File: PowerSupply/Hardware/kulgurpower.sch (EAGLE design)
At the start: 138 parts, among them M1 MST2V, M2 MST2V, M3 MST2V, M4 MST2V, X1 1727036, X2 2534-, X3 22-23-2031, X4 22-23-2031, X5 22-23-2021

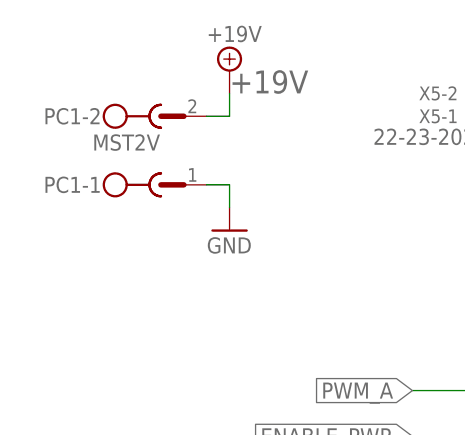
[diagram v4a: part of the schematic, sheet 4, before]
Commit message: Silkscreen fixes
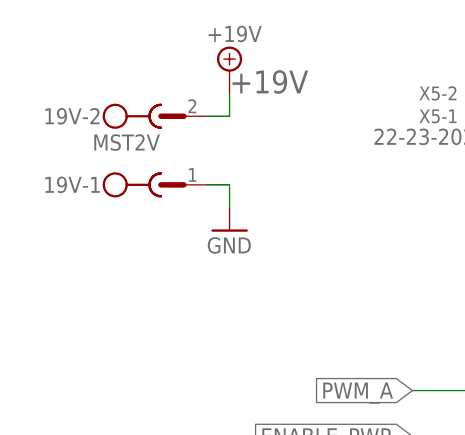
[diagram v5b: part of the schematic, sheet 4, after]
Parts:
- renumbered PC1 to 19V
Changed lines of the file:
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@@
 <part name="C15" library="rcl" deviceset="CPOL-EU" device="C/6032-28R"/>
 <part name="C30" library="rcl" deviceset="CPOL-EU" device="C/6032-28R"/>
-<part name="PC1" library="con-phoenix-508" deviceset="MST2V" device=""/>
+<part name="19V" library="con-phoenix-508" deviceset="MST2V" device=""/>
 <part name="SUPPLY6" library="supply2" deviceset="+18V" device="" value="+19V"/>
 <part name="GND52" library="supply1" deviceset="GND" device=""/>
@@
 <instance part="X5" gate="-2" x="101.6" y="157.48" rot="R180"/>
 <instance part="GND29" gate="1" x="106.68" y="149.86"/>
-<instance part="PC1" gate="-1" x="66.04" y="147.32"/>
-<instance part="PC1" gate="-2" x="66.04" y="154.94"/>
+<instance part="19V" gate="-1" x="66.04" y="147.32"/>
+<instance part="19V" gate="-2" x="66.04" y="154.94"/>
 <instance part="SUPPLY6" gate="+18V" x="73.66" y="160.02"/>
 <instance part="GND52" gate="1" x="73.66" y="142.24"/>
@@
 <pinref part="SUPPLY6" gate="+18V" pin="+18V"/>
 <label x="73.66" y="157.48" size="2.54" layer="95"/>
-<pinref part="PC1" gate="-2" pin="1"/>
+<pinref part="19V" gate="-2" pin="1"/>
 <wire x1="73.66" y1="154.94" x2="71.12" y2="154.94" width="0.4064" layer="91"/>
 </segment>
@@
 </segment>
 <segment>
-<pinref part="PC1" gate="-1" pin="1"/>
+<pinref part="19V" gate="-1" pin="1"/>
 <pinref part="GND52" gate="1" pin="GND"/>
 <wire x1="71.12" y1="147.32" x2="73.66" y2="147.32" width="0.1524" layer="91"/>

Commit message: Minor fixes to PCB
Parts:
- removed C13, C14: (no value), rcl:CPOL-EUC/6032-28R
- added C31, C35: (no value), rcl:CPOL-EUC/6032-28R
- added C36, C37: 15V, rcl:CPOL-EUC/6032-28R
- added C38: 15V, rcl:CPOL-EU175TMP-0810
- added C39: 15v, rcl:CPOL-EU175TMP-0810
- added D4: MBRS330T3, diode:MBRS330T3
- added PAD1, PAD2, PAD3, PAD4, PAD5, PAD6, PAD7, PAD8: (no value), wirepad:1,6/0,9
- C104, C113, C32: value 220n -> 0.1
- C3: value (none) -> 15V
- L1, L2: device inductors:DR73 -> inductors:DR125
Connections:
- net 5V renamed 5V_LDO
- new net +19V_CHG: D4.C, X2-14.KL, X2-16.KL
- new net N$2: D4.A
- net +19V: no longer X2-14.KL, X2-16.KL
- net +5V: now also C31.+, C35.+; no longer C13.+
- net GND: now also C31.-, C35.-, C36.-, C37.-, C38.-, C39.-; no longer C13.-, C14.-
- net SERVO: no longer C14.+
- net V+: now also C36.+, C37.+, C38.+, C39.+
- net VBAT0: no longer X2-1.KL, X2-2.KL
- net VBAT0_X: now also PAD1.P, PAD8.P, X2-1.KL, X2-2.KL
- net VBAT1: no longer X2-3.KL, X2-4.KL
- net VBAT1_X: now also PAD2.P, PAD7.P, X2-3.KL, X2-4.KL
- net VBAT2: no longer X2-5.KL, X2-6.KL
- net VBAT2_X: now also PAD3.P, PAD6.P, X2-5.KL, X2-6.KL
- net VBAT3: no longer X2-7.KL, X2-8.KL
- net VBAT3_X: now also PAD4.P, PAD5.P, X2-7.KL, X2-8.KL
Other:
- note added: "Hack! !ON! pin of MAX1614 is pulled up by default. Pulling it down enables power. This is achieved using shorting power socket with special tool. Diodes D1, D3 avoid 19V from adapter to flow into !ON! pin which is droven by MCU. D4 avoids flowing LiPo voltage to 19V socket."
- note removed: "Hack! !ON! pin of MAX1614 is pulled up by default. Pulling it down enables power. This is achieved using shorting power socket with special tool. Diodes avoid 19V from adapter to flow into !ON! pin which is droven by MCU."
- moved on the sheet: 19V-1, 19V-2, C1, C10, C113, C15, C16, C17, C2, C20, C21, C25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

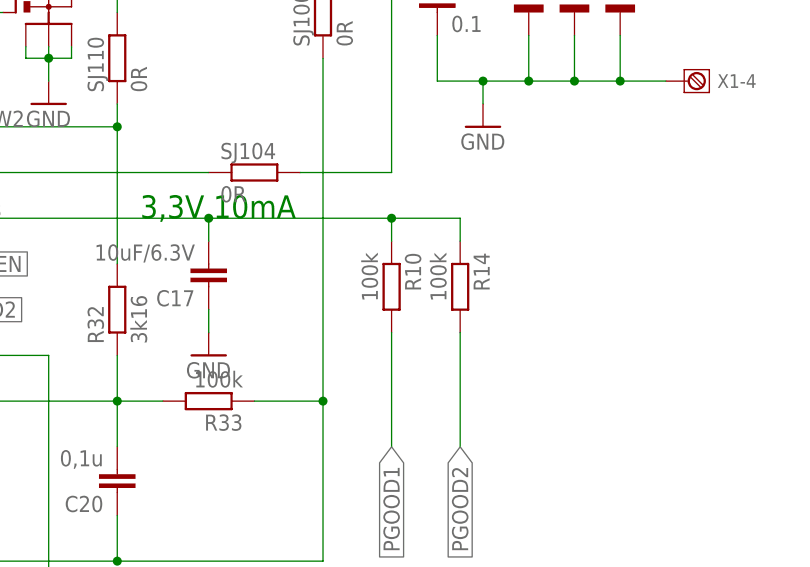
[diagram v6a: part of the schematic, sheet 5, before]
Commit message: Two resistors in ladder were swapped Nominals rised for pullup. Next power bill will be smaller!
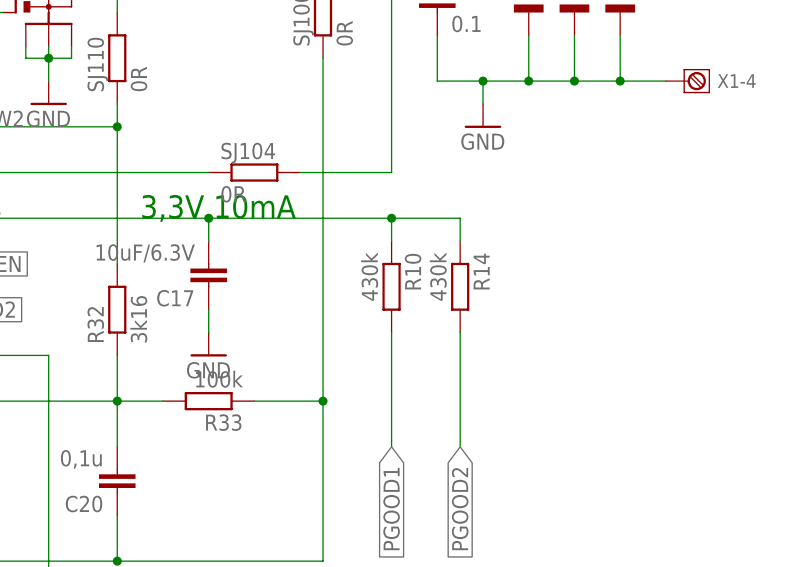
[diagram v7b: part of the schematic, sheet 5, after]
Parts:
- R10, R14: value 100k -> 430k
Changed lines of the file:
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@@
 <part name="X5" library="con-molex" deviceset="22-23-2021" device=""/>
 <part name="GND29" library="supply1" deviceset="GND" device=""/>
-<part name="R10" library="rcl" deviceset="R-EU_" device="R0603" value="100k"/>
-<part name="R14" library="rcl" deviceset="R-EU_" device="R0603" value="100k"/>
+<part name="R10" library="rcl" deviceset="R-EU_" device="R0603" value="430k"/>
+<part name="R14" library="rcl" deviceset="R-EU_" device="R0603" value="430k"/>
 <part name="C15" library="rcl" deviceset="CPOL-EU" device="C/6032-28R"/>
 <part name="C30" library="rcl" deviceset="CPOL-EU" device="C/6032-28R"/>

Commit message: PCB updates
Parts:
- C11, C18, C4, C7: value 0.1 -> 1n
- R25, R33: value 100k -> 3k9
- R31, R32: value 3k16 -> 10k
- R39: value 30k -> 24k
- R40: value 270k -> 143k
- R5: value 30k -> 24.3
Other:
- note added: "R1 = (VOUT -1.0) * R2 143 = 5.9 * 24.3"
- note removed: "R1 = (VOUT -1.0) * R2 270 = 9 * 30"
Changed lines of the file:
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@@
 <part name="U$4" library="SparkFun-AnalogIC" deviceset="ACS712" device=""/>
 <part name="GND5" library="supply1" deviceset="GND" device=""/>
-<part name="C7" library="rcl" deviceset="C-EU" device="C0603" value="0.1"/>
+<part name="C7" library="rcl" deviceset="C-EU" device="C0603" value="1n"/>
 <part name="GND15" library="supply1" deviceset="GND" device=""/>
 <part name="U$6" library="FDMS8558S" deviceset="FDMS8558S" device="" value="AON6500"/>
@@
 <part name="U$8" library="SparkFun-AnalogIC" deviceset="ACS712" device=""/>
 <part name="GND2" library="supply1" deviceset="GND" device=""/>
-<part name="C4" library="rcl" deviceset="C-EU" device="C0603" value="0.1"/>
+<part name="C4" library="rcl" deviceset="C-EU" device="C0603" value="1n"/>
 <part name="GND10" library="supply1" deviceset="GND" device=""/>
 <part name="U$9" library="FDMS8558S" deviceset="FDMS8558S" device="" value="AON6500"/>
@@
 <part name="U$11" library="SparkFun-AnalogIC" deviceset="ACS712" device=""/>
 <part name="GND12" library="supply1" deviceset="GND" device=""/>
-<part name="C11" library="rcl" deviceset="C-EU" device="C0603" value="0.1"/>
+<part name="C11" library="rcl" deviceset="C-EU" device="C0603" value="1n"/>
 <part name="GND18" library="supply1" deviceset="GND" device=""/>
 <part name="U$5" library="FDMS8558S" deviceset="FDMS8558S" device="" value="AON6500"/>
@@
 <part name="U$13" library="SparkFun-AnalogIC" deviceset="ACS712" device=""/>
 <part name="GND23" library="supply1" deviceset="GND" device=""/>
-<part name="C18" library="rcl" deviceset="C-EU" device="C0603" value="0.1"/>
+<part name="C18" library="rcl" deviceset="C-EU" device="C0603" value="1n"/>
 <part name="GND34" library="supply1" deviceset="GND" device=""/>
 <part name="PC" library="con-phoenix-508" deviceset="MST2V" device=""/>
@@
 <part name="GND22" library="SparkFun" deviceset="GND" device="" value="GND"/>
 <part name="R3" library="rcl" deviceset="R-EU_" device="R0603" value="300k"/>
-<part name="R39" library="rcl" deviceset="R-EU_" device="R0603" value="30k"/>
+<part name="R39" library="rcl" deviceset="R-EU_" device="R0603" value="24k"/>
 <part name="R23" library="rcl" deviceset="R-EU_" device="R0603" value="18k"/>
 <part name="R4" library="rcl" deviceset="R-EU_" device="R0603" value="30k"/>
-<part name="R5" library="rcl" deviceset="R-EU_" device="R0603" value="30k"/>
+<part name="R5" library="rcl" deviceset="R-EU_" device="R0603" value="24.3"/>
 <part name="R21" library="rcl" deviceset="R-EU_" device="R0603" value="120k"/>
-<part name="R40" library="rcl" deviceset="R-EU_" device="R0603" value="270k"/>
+<part name="R40" library="rcl" deviceset="R-EU_" device="R0603" value="143k"/>
 <part name="C5" library="rcl" deviceset="C-EU" device="C1210" value="10u"/>
 <part name="GND25" library="SparkFun" deviceset="GND" device=""/>
@@
 <part name="GND50" library="SparkFun" deviceset="GND" device=""/>
 <part name="SJ104" library="rcl" deviceset="R-EU_" device="R0603" value="0R"/>
-<part name="R31" library="rcl" deviceset="R-EU_" device="R0603" value="3k16"/>
-<part name="R32" library="rcl" deviceset="R-EU_" device="R0603" value="3k16"/>
-<part name="R25" library="rcl" deviceset="R-EU_" device="R0603" value="100k"/>
+<part name="R31" library="rcl" deviceset="R-EU_" device="R0603" value="10k"/>
+<part name="R32" library="rcl" deviceset="R-EU_" device="R0603" value="10k"/>
+<part name="R25" library="rcl" deviceset="R-EU_" device="R0603" value="3k9"/>
 <part name="C16" library="rcl" deviceset="C-EU" device="C0603" value="0,1u"/>
-<part name="R33" library="rcl" deviceset="R-EU_" device="R0603" value="100k"/>
+<part name="R33" library="rcl" deviceset="R-EU_" device="R0603" value="3k9"/>
 <part name="C20" library="rcl" deviceset="C-EU" device="C0603" value="0,1u"/>
 <part name="SJ114" library="rcl" deviceset="R-EU_" device="R0603" value="0R"/>
@@
 120 = 4 * 30</text>
 <text x="109.22" y="-12.7" size="1.778" layer="91">R1 = (VOUT -1.0) * R2
-270 = 9 * 30</text>
+143 = 5.9 * 24.3</text>
 </plain>
 <instances>
